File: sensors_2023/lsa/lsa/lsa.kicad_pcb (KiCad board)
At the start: 2 copper layers, 61.9 x 24.2 mm, 39 parts, among them J1 Conn_01x07_Male, U1 TCRT5000, U2 TCRT5000, U3 TCRT5000, U4 TCRT5000, U5 TCRT5000

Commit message: Resolve LSA wiring problem and fixed silkscreen, updated gerbers, fabrication outputs and 3D files for LSA
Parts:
- removed the kibuzzard-63708C00 at (116.0, 74.4)
- added kibuzzard-6394EC2D: G***, kibuzzard-6394EC2D, B.Cu at (117.0, 74.4)
- R1, R3, R5, R7, R9: value 150E -> 4.7k
- R10, R2, R4, R6, R8: value 4.7k -> 150R
- moved R6 5.48 mm to (113.3, 88.2), turned to 0 degrees
- moved R5 5.14 mm to (118.7, 88.2), turned to 0 degrees
- moved kibuzzard-63708D85 4.40 mm to (116.3, 85.8)
- moved R7 0.10 mm to (99.7, 77.0)
- moved R8 0.10 mm to (99.7, 82.2)
- turned U1 to -90 degrees
- turned U2 to -90 degrees
- turned U3 to -90 degrees
- turned U4 to -90 degrees
- turned U5 to -90 degrees
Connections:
- R1 pad 2: Net-(R1-Pad2) -> /A0_36
- R10 pad 1: /A4_32 -> Net-(R10-Pad1)
- R2 pad 1: /A0_36 -> Net-(R2-Pad1)
- R3 pad 2: Net-(R3-Pad2) -> /A1_39
- R4 pad 1: /A1_39 -> Net-(R4-Pad1)
- R5 pad 2: Net-(R5-Pad2) -> /A2_34
- R6 pad 1: /A2_34 -> Net-(R6-Pad1)
- R7 pad 2: Net-(R7-Pad2) -> /A3_35
- R8 pad 1: /A3_35 -> Net-(R8-Pad1)
- R9 pad 2: Net-(R9-Pad2) -> /A4_32
- U1 pad A: GND -> Net-(R2-Pad1)
- U1 pad CATH: Net-(R1-Pad2) -> GND
- U1 pad COLL: GND -> /A0_36
- U1 pad E: /A0_36 -> GND
- U2 pad A: GND -> Net-(R4-Pad1)
- U2 pad CATH: Net-(R3-Pad2) -> GND
- U2 pad COLL: GND -> /A1_39
- U2 pad E: /A1_39 -> GND
- U3 pad A: GND -> Net-(R6-Pad1)
- U3 pad CATH: Net-(R5-Pad2) -> GND
- U3 pad COLL: GND -> /A2_34
- U3 pad E: /A2_34 -> GND
- U4 pad A: GND -> Net-(R8-Pad1)
- U4 pad CATH: Net-(R7-Pad2) -> GND
- U4 pad COLL: GND -> /A3_35
- U4 pad E: /A3_35 -> GND
- U5 pad A: GND -> Net-(R10-Pad1)
- U5 pad CATH: Net-(R9-Pad2) -> GND
- U5 pad COLL: GND -> /A4_32
- U5 pad E: /A4_32 -> GND
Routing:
- net +3V3: track 93.7 -> 114.6 mm
- net Net-(R5-Pad2): track 17.5 -> 0.00 mm
- net /A0_36: track 43.7 -> 27.8 mm
- net Net-(R6-Pad1): track 0.00 -> 9.45 mm
- net /A4_32: track 28.2 -> 19.8 mm
- net Net-(R2-Pad1): track 0.00 -> 7.88 mm
- net Net-(R1-Pad2): track 7.79 -> 0.00 mm
- net Net-(R8-Pad1): track 0.00 -> 7.12 mm
- net Net-(R7-Pad2): track 7.06 -> 0.00 mm
- net Net-(R3-Pad2): track 4.98 -> 0.00 mm
- net Net-(R9-Pad2): track 4.83 -> 0.00 mm
- net /A1_39: track 26.7 -> 22.1 mm
- net /A2_34: track 23.7 -> 19.5 mm
- net /A3_35: track 21.9 -> 18.0 mm
- net Net-(R4-Pad1): track 0.00 -> 3.80 mm
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
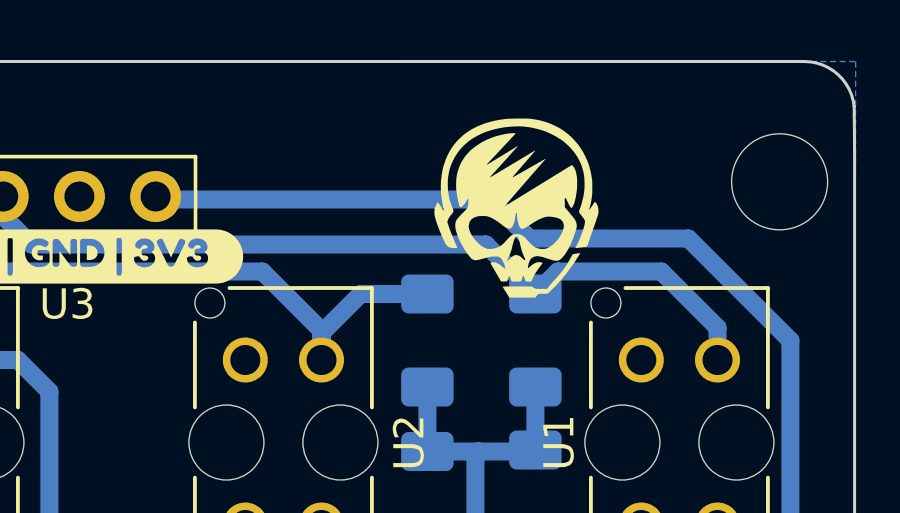
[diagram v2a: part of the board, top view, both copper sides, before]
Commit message: Update LSA and SRA board after hardware testing
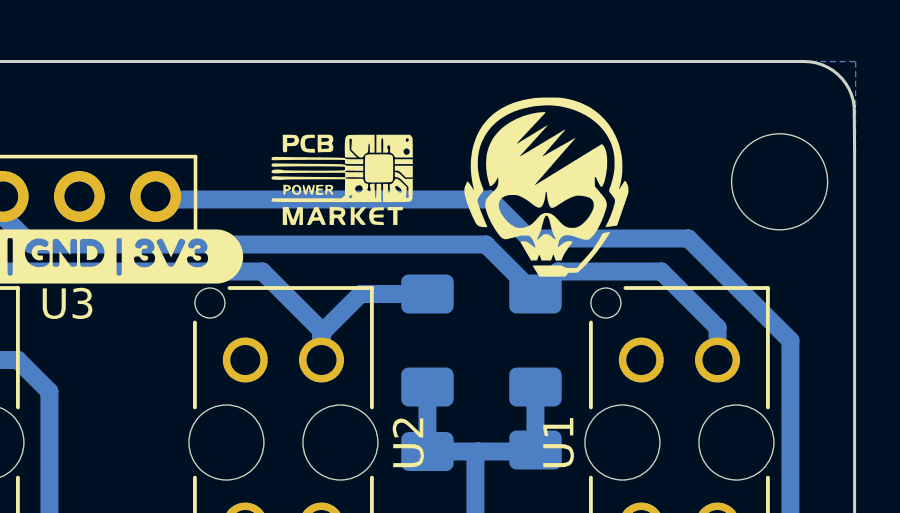
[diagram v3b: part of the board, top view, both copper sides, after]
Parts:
- added G***: LOGO, logos:pcb_power_small, F.Cu at (130.1, 71.7)
- moved G*** 1.22 mm to (136.8, 72.1)
- moved kibuzzard-63708D85 0.14 mm to (116.2, 85.7)
